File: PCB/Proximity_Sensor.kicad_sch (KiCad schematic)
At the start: 8 parts, among them U7 VL6180XV0NR_1

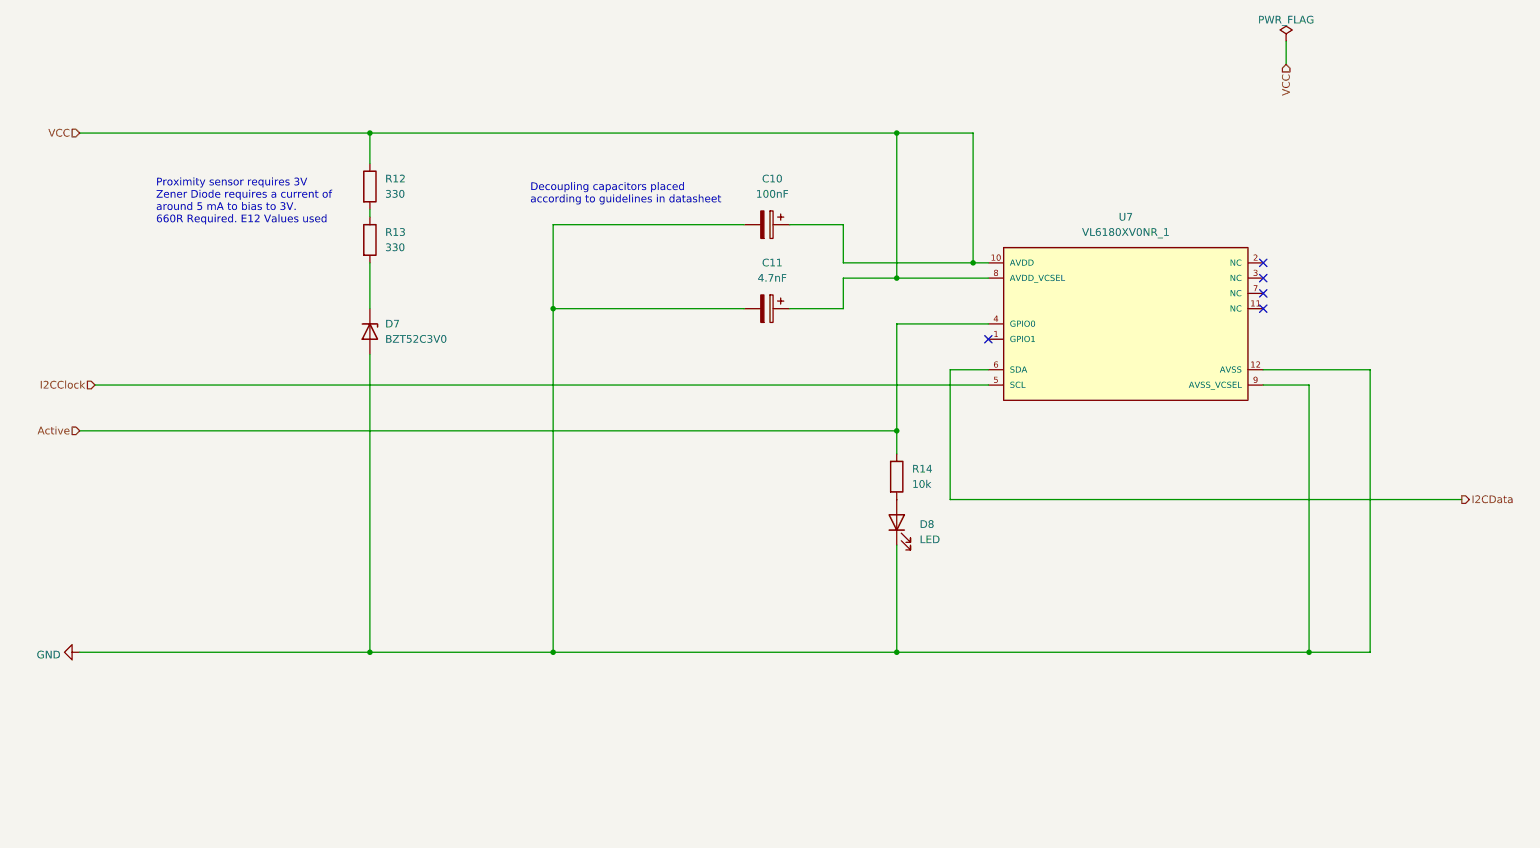
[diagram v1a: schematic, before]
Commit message: Mostly addressed issues with Sensing subsystem
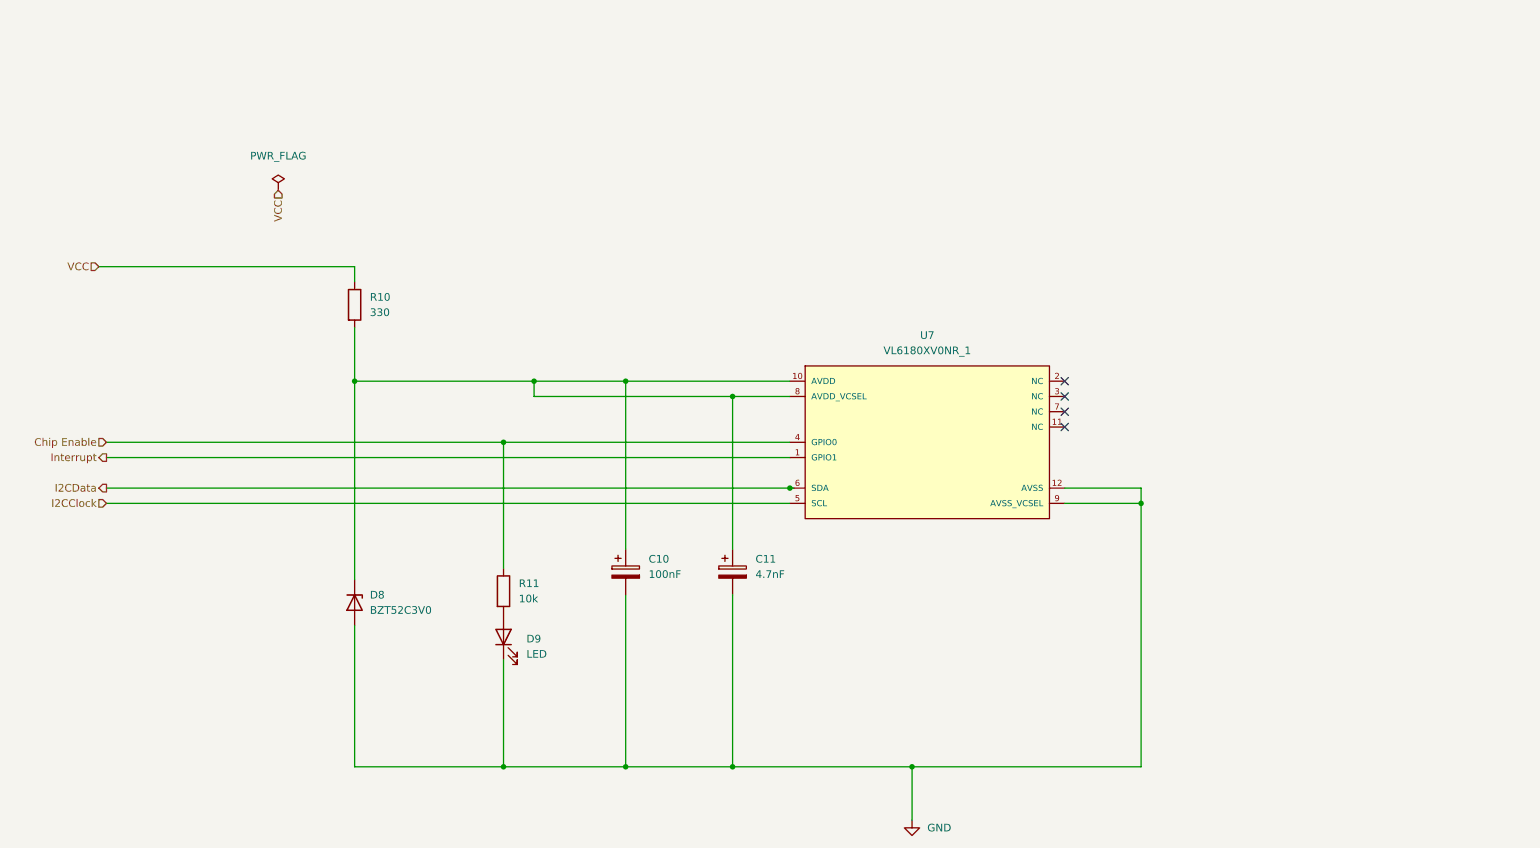
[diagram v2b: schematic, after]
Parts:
- removed D7: BZT52C3V0, Diode_SMD:D_SOD-123, symbol Diode:BZT52Bxx
- removed D8: LED, LED_SMD:LED_0603_1608Metric, symbol Device:LED
- removed R12, R13: 330, Resistor_SMD:R_0402_1005Metric, symbol Device:R
- removed R14: 10k, Resistor_SMD:R_0402_1005Metric, symbol Device:R
- added D8: BZT52C3V0, Diode_SMD:D_SOD-123, symbol Diode:BZT52Bxx
- added D9: LED, LED_SMD:LED_0603_1608Metric, symbol Device:LED
- added R10: 330, Resistor_SMD:R_0402_1005Metric, symbol Device:R
- added R11: 10k, Resistor_SMD:R_0402_1005Metric, symbol Device:R
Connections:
- net GND: now also D8.2 (A), D9.1 (K)
- net VCC: now also R10.1; no longer C10.1, C11.1, U7.10 (AVDD), U7.8 (AVDD_VCSEL)
- net Interrupt: now reaches U7.1 (GPIO1)
- net Active renamed Chip Enable
- net Chip Enable: now also R11.1
- new net: C10.1, C11.1, D8.1 (K), R10.2, U7.10 (AVDD), U7.8 (AVDD_VCSEL)
- new net: D9.2 (A), R11.2
- no-connect marks 5 -> 4
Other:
- note removed: "Decoupling capacitors placed according to guidelines in datasheet"
- note removed: "Proximity sensor requires 3V Zener Diode requires a current of around 5 mA to bias to 3V. 660R Required. E12 Values used"

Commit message: Prepare PCB
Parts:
- C10: JLC Part # C307331 -> C1525; LCSC (none) -> C1525; Price 0.0065 -> (none)
- C11: JLC Part # C1538 -> C1538; LCSC (none) -> C1538
- D8: JLC Part # C266562 -> C266562; LCSC (none) -> C266562
- D9: value LED -> RLED; LCSC (none) -> C2286
- R10: JLC Part # C25104 -> C25104; LCSC (none) -> C25104
- R11: LCSC (none) -> C25744
- U7: LCSC (none) -> C2655167
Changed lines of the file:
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@@
       (effects (font (size 1.27 1.27)) hide)
     )
-    (property "JLC Part #" " C1538" (id 5) (at 145.415 111.125 0)
+    (property "JLC Part #" "C1538" (id 5) (at 145.415 111.125 0)
       (effects (font (size 1.27 1.27)) hide)
     )
@@
       (effects (font (size 1.27 1.27)) hide)
     )
+    (property "LCSC" "C1538" (id 7) (at 145.415 111.125 0)
+      (effects (font (size 1.27 1.27)) hide)
+    )
     (pin "1")
     (pin "2")
@@
   (symbol (lib_id "Device:LED") (at 107.315 121.92 90) (unit 1)
     (in_bom yes) (on_board yes) (fields_autoplaced)
-    (property "Reference" "D9" (id 0) (at 111.125 122.2374 90)
+    (property "Reference" "D9" (id 0) (at 110.236 122.6728 90)
       (effects (font (size 1.27 1.27)) (justify right))
     )
-    (property "Value" "LED" (id 1) (at 111.125 124.7774 90)
+    (property "Value" "RLED" (id 1) (at 110.236 125.2097 90)
       (effects (font (size 1.27 1.27)) (justify right))
     )
@@
       (effects (font (size 1.27 1.27)) hide)
     )
+    (property "LCSC" "C2286" (id 7) (at 107.315 121.92 0)
+      (effects (font (size 1.27 1.27)) hide)
+    )
     (pin "1")
     (pin "2")
@@
       (effects (font (size 1.27 1.27)) hide)
     )
-    (property "JLC Part #" " C266562" (id 5) (at 82.55 116.205 0)
+    (property "JLC Part #" "C266562" (id 5) (at 82.55 116.205 0)
       (effects (font (size 1.27 1.27)) hide)
     )
@@
       (effects (font (size 1.27 1.27)) hide)
     )
+    (property "LCSC" "C266562" (id 7) (at 82.55 116.205 0)
+      (effects (font (size 1.27 1.27)) hide)
+    )
     (pin "1")
     (pin "2")
@@
       (effects (font (size 1.27 1.27)) hide)
     )
+    (property "LCSC" "C25744" (id 8) (at 107.315 114.3 0)
+      (effects (font (size 1.27 1.27)) hide)
+    )
     (pin "1")
     (pin "2")
@@
       (effects (font (size 1.27 1.27)) hide)
     )
-    (property "JLC Part #" " C25104" (id 5) (at 82.55 66.675 0)
+    (property "JLC Part #" "C25104" (id 5) (at 82.55 66.675 0)
       (effects (font (size 1.27 1.27)) hide)
     )
     (property "Price" "0.0007" (id 6) (at 82.55 66.675 0)
+      (effects (font (size 1.27 1.27)) hide)
+    )
+    (property "LCSC" "C25104" (id 7) (at 82.55 66.675 0)
       (effects (font (size 1.27 1.27)) hide)
     )
@@
     )
     (property "Price" "1.9575" (id 29) (at 152.4 79.375 0)
+      (effects (font (size 1.27 1.27)) hide)
+    )
+    (property "LCSC" "C2655167" (id 30) (at 152.4 79.375 0)
       (effects (font (size 1.27 1.27)) hide)
     )
@@
       (effects (font (size 1.27 1.27)) hide)
     )
-    (property "JLC Part #" " C307331" (id 5) (at 127.635 111.125 0)
-      (effects (font (size 1.27 1.27)) hide)
-    )
-    (property "Price" "0.0065" (id 6) (at 127.635 111.125 0)
-      (effects (font (size 1.27 1.27)) hide)
-    )
+    (property "JLC Part #" "C1525" (id 5) (at 127.635 111.125 0)
+      (effects (font (size 1.27 1.27)) hide)
+    )
+    (property "Price" "" (id 6) (at 127.635 111.125 0)
+      (effects (font (size 1.27 1.27)) hide)
+    )
+    (property "LCSC" "C1525" (id 7) (at 127.635 111.125 0)
+      (effects (font (size 1.27 1.27)) hide)
+    )

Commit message: Final Schematic changes
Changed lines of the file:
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@@
   (junction (at 82.55 79.375) (diameter 0) (color 0 0 0 0)
-  )
-  (junction (at 154.94 97.155) (diameter 0) (color 0 0 0 0)
   )
   (junction (at 145.415 143.51) (diameter 0) (color 0 0 0 0)
@@
     (stroke (width 0) (type default) (color 0 0 0 0))
   )
-  (wire (pts (xy 155.575 97.155) (xy 154.94 97.155))
-    (stroke (width 0) (type default) (color 0 0 0 0))
-  )
